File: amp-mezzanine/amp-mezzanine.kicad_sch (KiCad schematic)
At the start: 16 parts, among them J1 LOGIC_IN, J2 I2C, J3 PWR_A, J4 PWR_B

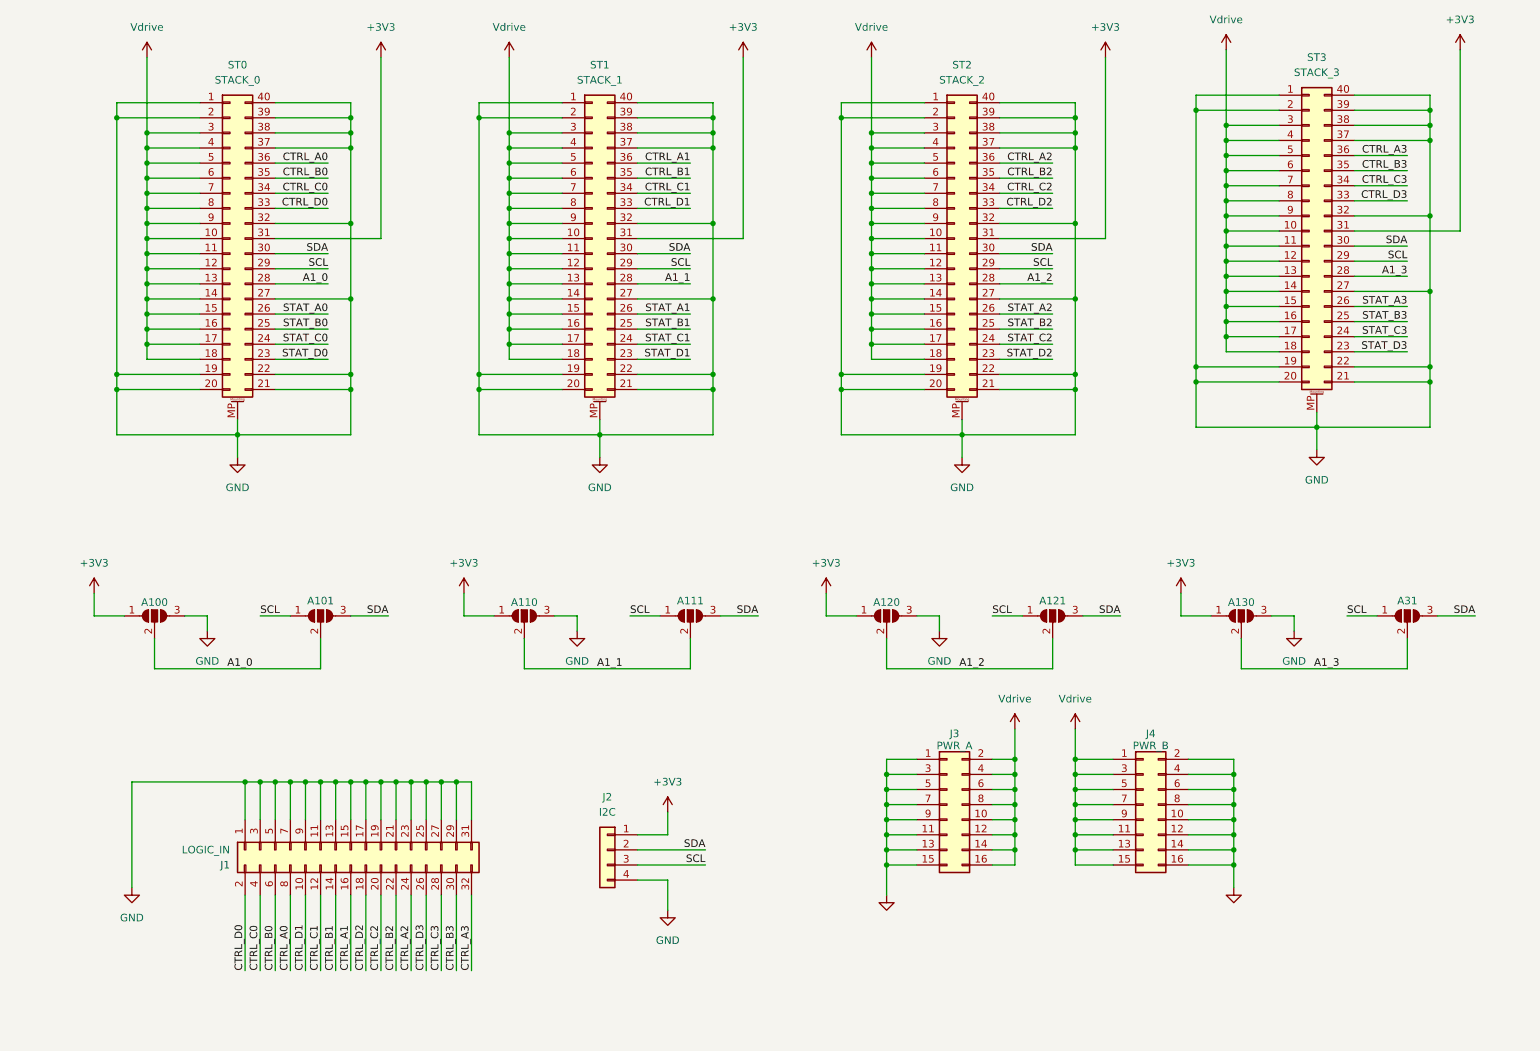
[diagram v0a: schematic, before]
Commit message: Added DS2484 to mezzanine board
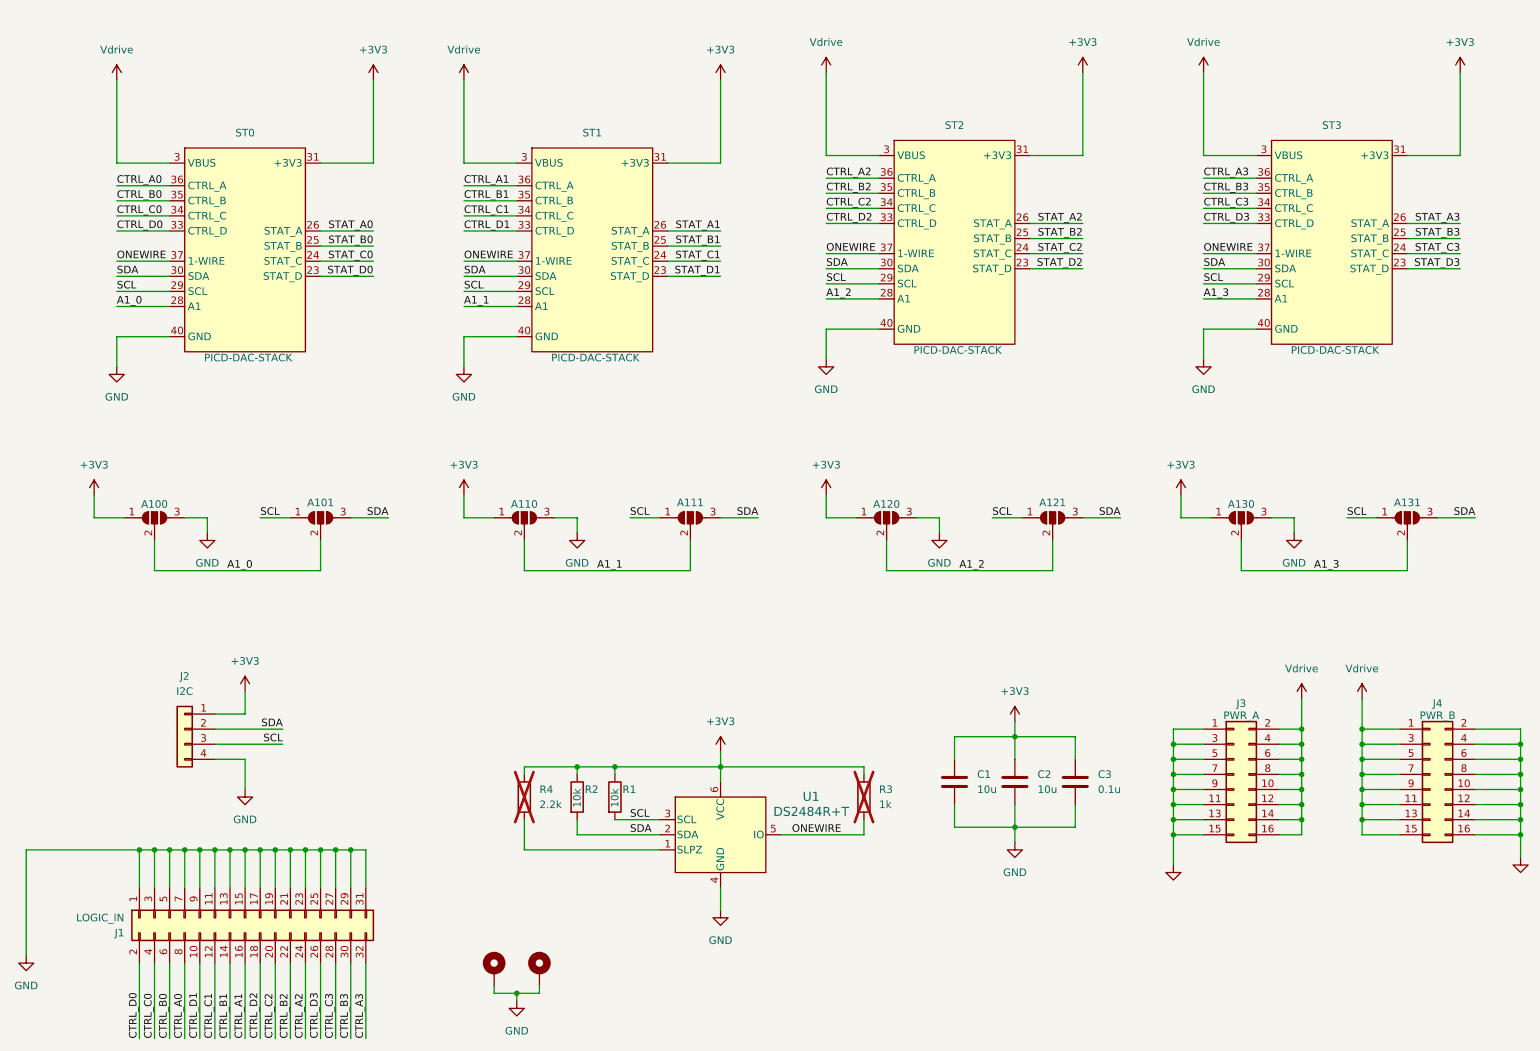
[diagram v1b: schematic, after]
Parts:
- removed ST0: STACK_0, project_footprints:PICCDAC-AMPHENOL-10132797-045100LF, symbol Connector_Generic_MountingPin:Conn_02x20_Counter_Clockwise_MountingPin
- removed ST1: STACK_1, project_footprints:PICCDAC-AMPHENOL-10132797-045100LF, symbol Connector_Generic_MountingPin:Conn_02x20_Counter_Clockwise_MountingPin
- removed ST2: STACK_2, project_footprints:PICCDAC-AMPHENOL-10132797-045100LF, symbol Connector_Generic_MountingPin:Conn_02x20_Counter_Clockwise_MountingPin
- removed ST3: STACK_3, project_footprints:PICCDAC-AMPHENOL-10132797-045100LF, symbol Connector_Generic_MountingPin:Conn_02x20_Counter_Clockwise_MountingPin
- added C1, C2: 10u, Capacitor_SMD:C_0805_2012Metric, symbol Device:C
- added C3: 0.1u, Capacitor_SMD:C_0805_2012Metric, symbol Device:C
- added H1, H2: MountingHole_Pad, MountingHole:MountingHole_3.2mm_M3_Pad_Via, symbol Mechanical:MountingHole_Pad
- added R1, R2: 10k, Resistor_SMD:R_0402_1005Metric, symbol Device:R
- added R3: 1k, Resistor_SMD:R_0402_1005Metric, symbol Device:R
- added R4: 2.2k, Resistor_SMD:R_0402_1005Metric, symbol Device:R
- added ST0, ST1, ST2, ST3: PICD-DAC-STACK, project_footprints:PICCDAC-AMPHENOL-10132797-045100LF, symbol project_symbols:PICD-AMP-STACK
- added U1: DS2484R+T, project_footprints:21-0058I_MXM-L, symbol project_symbols:DS2484R+T
- A100, A121: value SolderJumper_3_Open -> R
- A101, A111, A120, A130: value SolderJumper_3_Open -> NC
- A110: value SolderJumper_3_Open -> L
- A131: renamed from A31; value SolderJumper_3_Open -> L
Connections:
- net +3V3: now also C1.1, C2.1, C3.1, R1.1, R2.1, R3.1, R4.1, ST0.31 (+3V3), ST1.31 (+3V3), ST2.31 (+3V3), ST3.31 (+3V3), U1.6 (VCC)
- net A1_0: now also ST0.28 (A1)
- net A1_1: now also ST1.28 (A1)
- net A1_2: now also ST2.28 (A1)
- net A1_3: now also ST3.28 (A1)
- net CTRL_A0: now also ST0.36 (CTRL_A)
- net CTRL_A1: now also ST1.36 (CTRL_A)
- net CTRL_A2: now also ST2.36 (CTRL_A)
- net CTRL_A3: now also ST3.36 (CTRL_A)
- net CTRL_B0: now also ST0.35 (CTRL_B)
- net CTRL_B1: now also ST1.35 (CTRL_B)
- net CTRL_B2: now also ST2.35 (CTRL_B)
- net CTRL_B3: now also ST3.35 (CTRL_B)
- net CTRL_C0: now also ST0.34 (CTRL_C)
- net CTRL_C1: now also ST1.34 (CTRL_C)
- net CTRL_C2: now also ST2.34 (CTRL_C)
- net CTRL_C3: now also ST3.34 (CTRL_C)
- net CTRL_D0: now also ST0.33 (CTRL_D)
- net CTRL_D1: now also ST1.33 (CTRL_D)
- net CTRL_D2: now also ST2.33 (CTRL_D)
- net CTRL_D3: now also ST3.33 (CTRL_D)
- net GND: now also C1.2, C2.2, C3.2, H1.1, H2.1, ST0.1 (GND), ST0.19 (GND), ST0.2 (GND), ST0.20 (GND), ST0.21 (GND), ST0.22 (GND), ST0.27 (GND), ST0.32 (GND), ST0.38 (GND), ST0.39 (GND), ST0.40 (GND), ST0.MP (GND), ST1.1 (GND), ST1.19 (GND), ST1.2 (GND), ST1.20 (GND), ST1.21 (GND), ST1.22 (GND), ST1.27 (GND), ST1.32 (GND), ST1.38 (GND), ST1.39 (GND), ST1.40 (GND), ST1.MP (GND), ST2.1 (GND), ST2.19 (GND), ST2.2 (GND), ST2.20 (GND), ST2.21 (GND), ST2.22 (GND), ST2.27 (GND), ST2.32 (GND), ST2.38 (GND), ST2.39 (GND), ST2.40 (GND), ST2.MP (GND), ST3.1 (GND), ST3.19 (GND), ST3.2 (GND), ST3.20 (GND), ST3.21 (GND), ST3.22 (GND), ST3.27 (GND), ST3.32 (GND), ST3.38 (GND), ST3.39 (GND), ST3.40 (GND), ST3.MP (GND), U1.4 (GND)
- net SCL: now also R1.2, ST0.29 (SCL), ST1.29 (SCL), ST2.29 (SCL), ST3.29 (SCL), U1.3 (SCL)
- net SDA: now also R2.2, ST0.30 (SDA), ST1.30 (SDA), ST2.30 (SDA), ST3.30 (SDA), U1.2 (SDA)
- net STAT_A0: now also ST0.26 (STAT_A)
- net STAT_A1: now also ST1.26 (STAT_A)
- net STAT_A2: now also ST2.26 (STAT_A)
- net STAT_A3: now also ST3.26 (STAT_A)
- net STAT_B0: now also ST0.25 (STAT_B)
- net STAT_B1: now also ST1.25 (STAT_B)
- net STAT_B2: now also ST2.25 (STAT_B)
- net STAT_B3: now also ST3.25 (STAT_B)
- net STAT_C0: now also ST0.24 (STAT_C)
- net STAT_C1: now also ST1.24 (STAT_C)
- net STAT_C2: now also ST2.24 (STAT_C)
- net STAT_C3: now also ST3.24 (STAT_C)
- net STAT_D0: now also ST0.23 (STAT_D)
- net STAT_D1: now also ST1.23 (STAT_D)
- net STAT_D2: now also ST2.23 (STAT_D)
- net STAT_D3: now also ST3.23 (STAT_D)
- net Vdrive renamed VBUS
- net VBUS: now also ST0.10 (VBUS), ST0.11 (VBUS), ST0.12 (VBUS), ST0.13 (VBUS), ST0.14 (VBUS), ST0.15 (VBUS), ST0.16 (VBUS), ST0.17 (VBUS), ST0.18 (VBUS), ST0.3 (VBUS), ST0.4 (VBUS), ST0.5 (VBUS), ST0.6 (VBUS), ST0.7 (VBUS), ST0.8 (VBUS), ST0.9 (VBUS), ST1.10 (VBUS), ST1.11 (VBUS), ST1.12 (VBUS), ST1.13 (VBUS), ST1.14 (VBUS), ST1.15 (VBUS), ST1.16 (VBUS), ST1.17 (VBUS), ST1.18 (VBUS), ST1.3 (VBUS), ST1.4 (VBUS), ST1.5 (VBUS), ST1.6 (VBUS), ST1.7 (VBUS), ST1.8 (VBUS), ST1.9 (VBUS), ST2.10 (VBUS), ST2.11 (VBUS), ST2.12 (VBUS), ST2.13 (VBUS), ST2.14 (VBUS), ST2.15 (VBUS), ST2.16 (VBUS), ST2.17 (VBUS), ST2.18 (VBUS), ST2.3 (VBUS), ST2.4 (VBUS), ST2.5 (VBUS), ST2.6 (VBUS), ST2.7 (VBUS), ST2.8 (VBUS), ST2.9 (VBUS), ST3.10 (VBUS), ST3.11 (VBUS), ST3.12 (VBUS), ST3.13 (VBUS), ST3.14 (VBUS), ST3.15 (VBUS), ST3.16 (VBUS), ST3.17 (VBUS), ST3.18 (VBUS), ST3.3 (VBUS), ST3.4 (VBUS), ST3.5 (VBUS), ST3.6 (VBUS), ST3.7 (VBUS), ST3.8 (VBUS), ST3.9 (VBUS)
- new net: R4.2, U1.1 (SLPZ)
- new net ONEWIRE: R3.2, ST0.37 (1-WIRE), ST1.37 (1-WIRE), ST2.37 (1-WIRE), ST3.37 (1-WIRE), U1.5 (IO)
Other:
- company: (none) -> ${COMPANY}
- title: (none) -> ${PRJ_TITLE}
- moved on the sheet: A100, A101, A110, A111, A120, A121, A130, A131, J1, J2, J3, J4

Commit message: Modified DAC, AMP v2 and Mezzanine to support AMP v3. Finished AMP v3 design.
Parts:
- removed J1: LOGIC_IN, Connector_PinHeader_2.54mm:PinHeader_2x16_P2.54mm_Vertical, symbol Connector_Generic:Conn_02x16_Odd_Even
- added J1: LOGIC_IN, Connector_PinHeader_2.54mm:PinHeader_2x17_P2.54mm_Vertical, symbol Connector_Generic:Conn_02x17_Odd_Even
- J2, J3, J4: now not fitted
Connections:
- net CTRL_A0: now also J1.27 (Pin_27)
- net CTRL_A1: now also J1.19 (Pin_19)
- net CTRL_A2: now also J1.11 (Pin_11)
- net CTRL_A3: now also J1.3 (Pin_3)
- net CTRL_B0: now also J1.29 (Pin_29)
- net CTRL_B1: now also J1.21 (Pin_21)
- net CTRL_B2: now also J1.13 (Pin_13)
- net CTRL_B3: now also J1.5 (Pin_5)
- net CTRL_C0: now also J1.31 (Pin_31)
- net CTRL_C1: now also J1.23 (Pin_23)
- net CTRL_C2: now also J1.15 (Pin_15)
- net CTRL_C3: now also J1.7 (Pin_7)
- net CTRL_D0: now also J1.33 (Pin_33)
- net CTRL_D1: now also J1.25 (Pin_25)
- net CTRL_D2: now also J1.17 (Pin_17)
- net CTRL_D3: now also J1.9 (Pin_9)
- net GND: now also J1.10 (Pin_10), J1.12 (Pin_12), J1.14 (Pin_14), J1.16 (Pin_16), J1.18 (Pin_18), J1.2 (Pin_2), J1.20 (Pin_20), J1.22 (Pin_22), J1.24 (Pin_24), J1.26 (Pin_26), J1.28 (Pin_28), J1.30 (Pin_30), J1.32 (Pin_32), J1.34 (Pin_34), J1.4 (Pin_4), J1.6 (Pin_6), J1.8 (Pin_8); no longer ST0.38 (GND), ST1.38 (GND), ST2.38 (GND), ST3.38 (GND)
- new net EN: J1.1 (Pin_1), ST0.38 (EN), ST1.38 (EN), ST2.38 (EN), ST3.38 (EN)
